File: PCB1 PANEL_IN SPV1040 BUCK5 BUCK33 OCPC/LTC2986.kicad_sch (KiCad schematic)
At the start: 1 part, among them U15 LTC2986HLX_PBF

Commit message: s
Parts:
- removed U15: LTC2986HLX_PBF, LTC2986HLX_PBF:QFP50P900X900X160-48N, symbol LTC2986:LTC2986HLX_PBF
- added C1, C4, C5, C6: 10uF, symbol Device:C
- added C2: 47uF, symbol Device:C
- added C3: 0.1uF, symbol Device:C
- added C7, C8: 1uF, symbol Device:C
- added U1: LTC2986HLX-PBF, LX_48_ADI, symbol 2025-01-09_17-24-37:LTC2986HLX-PBF
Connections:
- net GND: now also C1.2, C2.2, C3.2, C4.2, C5.2, C6.2, C7.2, C8.2, U1.1 (GND), U1.12 (GND), U1.15 (GND), U1.26 (GND), U1.27 (GND), U1.28 (GND), U1.29 (GND), U1.3 (GND), U1.30 (GND), U1.31 (GND), U1.32 (GND), U1.33 (GND), U1.34 (GND), U1.35 (GND), U1.36 (COM), U1.44 (GND), U1.5 (GND), U1.7 (GND), U1.9 (GND)
- new net: C8.1, U1.11 (VREFBYP)
- new net: C7.1, U1.13 (VREFOUT), U1.14 (VREFP)
- new net: C4.1, U1.43 (LDO)
- new net: C6.1, U1.46 (Q3)
- new net: C5.1, U1.47 (Q2), U1.48 (Q1)
- new net CS: U1.41 (*CS)
- new net INTERRUPT: U1.37 (INTERRUPT)
- new net MISO: U1.40 (SDI)
- new net MOSI: U1.39 (SDO)
- new net RST: U1.42 (*RESET)
- new net SCK: U1.38 (SCK)
- new net VDD: C1.1, C2.1, C3.1, U1.2 (VDD), U1.4 (VDD), U1.45 (VDD), U1.6 (VDD), U1.8 (VDD)
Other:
- note added: "1. RESET PIN and CS PIN are ACTIVE LOW 2. INTERRUPT pin here is an outpin which gives LOW when the conversion cycle in the process and HIGH on the conclusion"

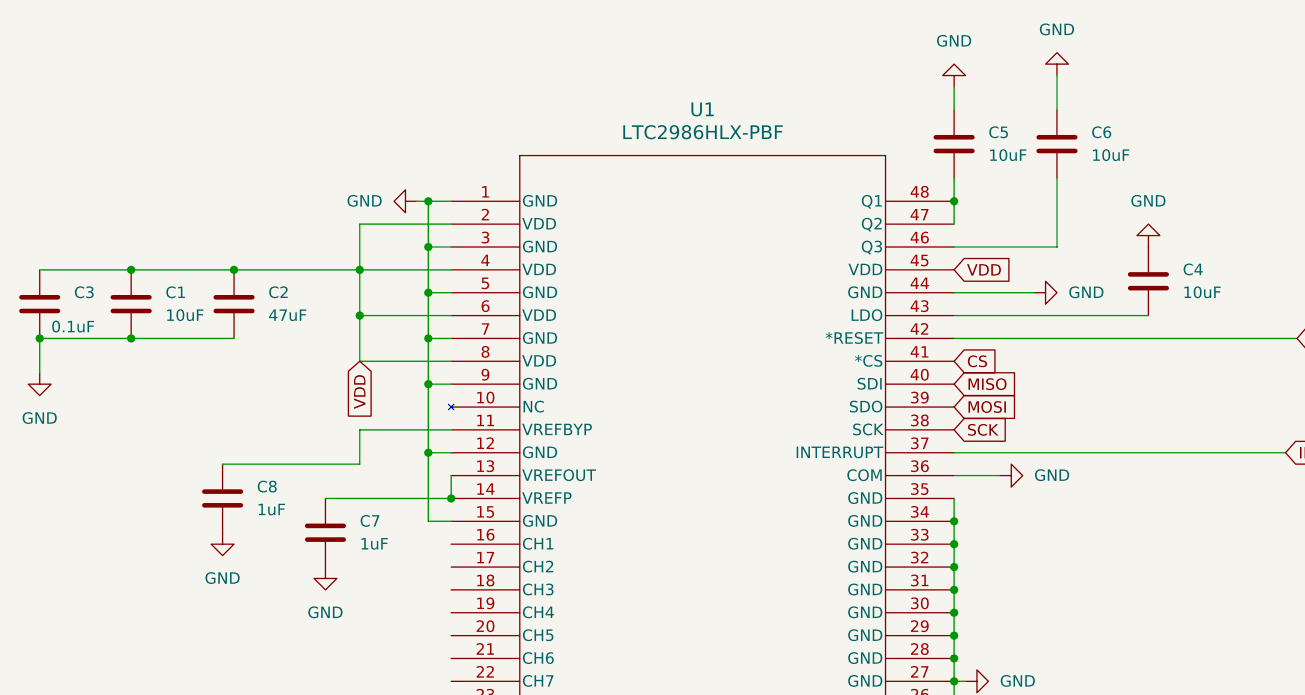
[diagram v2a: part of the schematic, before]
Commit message: Relabeling according to standards
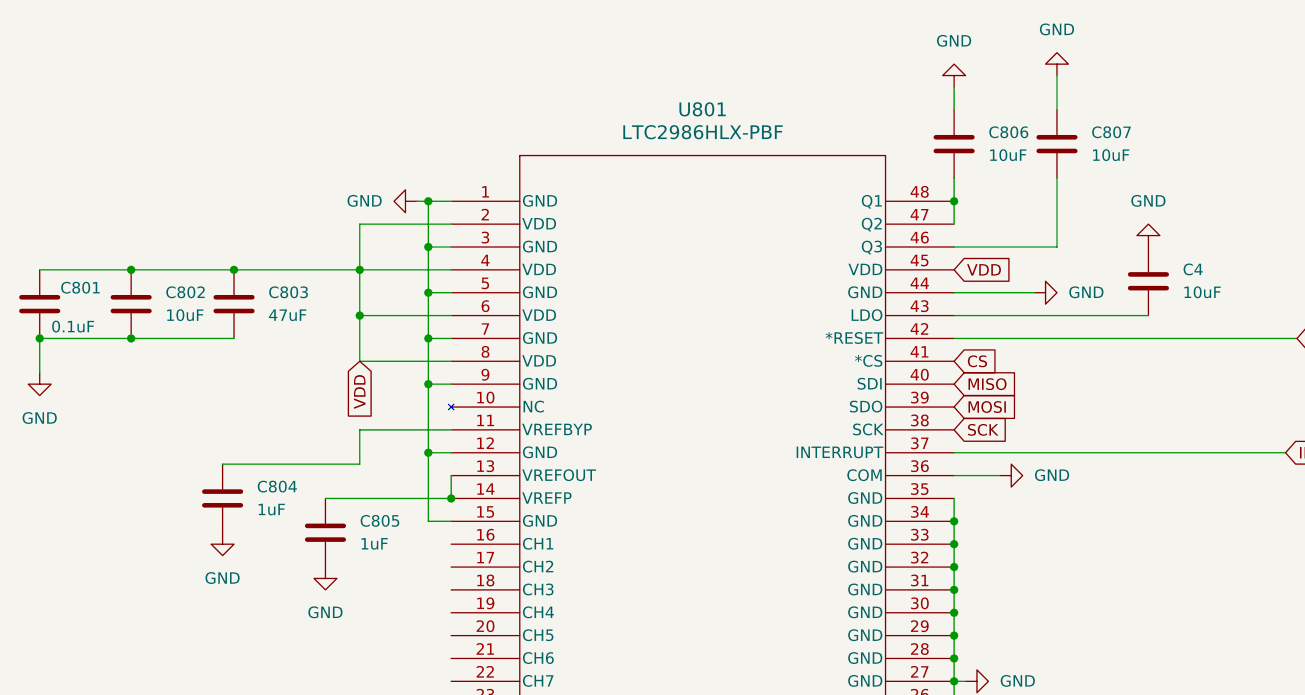
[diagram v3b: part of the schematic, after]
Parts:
- U801: renamed from U1; footprint LX_48_ADI -> (none)
- renumbered C3 to C801, C1 to C802, C2 to C803, C8 to C804, C7 to C805, C5 to C806, C6 to C807
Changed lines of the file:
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@@
 		(dnp no)
 		(fields_autoplaced yes)
-		(property "Reference" "#PWR01"
+		(property "Reference" "#PWR0111"
 			(at 97.79 38.1 0)
 			(effects
@@
 		(instances
 			(project ""
+				(path "/494c9d9f-6b33-4248-a813-27ffaaa929bd/81ba6a5a-e21d-4cec-83f0-5d840c1285ed"
+					(reference "#PWR0111")
+					(unit 1)
+				)
+			)
+			(project ""
 				(path "/e5df9c19-46f5-47d3-b6f4-a0778a1551ae"
 					(reference "#PWR01")
@@
 		(dnp no)
 		(fields_autoplaced yes)
-		(property "Reference" "U1"
+		(property "Reference" "U801"
 			(at 135.89 27.94 0)
 			(effects
@@
 			)
 		)
-		(property "Footprint" "LX_48_ADI"
+		(property "Footprint" ""
 			(at 107.95 38.1 0)
 			(effects
@@
 		(instances
 			(project ""
+				(path "/494c9d9f-6b33-4248-a813-27ffaaa929bd/81ba6a5a-e21d-4cec-83f0-5d840c1285ed"
+					(reference "U801")
+					(unit 1)
+				)
+			)
+			(project ""
 				(path "/e5df9c19-46f5-47d3-b6f4-a0778a1551ae"
 					(reference "U1")
@@
 		(dnp no)
 		(fields_autoplaced yes)
-		(property "Reference" "#PWR05"
+		(property "Reference" "#PWR0155"
 			(at 185.42 36.83 0)
 			(effects
@@
 		)
 		(instances
+			(project ""
+				(path "/494c9d9f-6b33-4248-a813-27ffaaa929bd/81ba6a5a-e21d-4cec-83f0-5d840c1285ed"
+					(reference "#PWR0155")
+					(unit 1)
+				)
+			)
 			(project "LTC2986"
 				(path "/e5df9c19-46f5-47d3-b6f4-a0778a1551ae"
@@
 		(dnp no)
 		(fields_autoplaced yes)
-		(property "Reference" "C6"
+		(property "Reference" "C807"
 			(at 179.07 30.4799 0)
 			(effects
@@
 		)
 		(instances
+			(project ""
+				(path "/494c9d9f-6b33-4248-a813-27ffaaa929bd/81ba6a5a-e21d-4cec-83f0-5d840c1285ed"
+					(reference "C807")
+					(unit 1)
+				)
+			)
 			(project "LTC2986"
 				(path "/e5df9c19-46f5-47d3-b6f4-a0778a1551ae"
@@
 		(dnp no)
 		(fields_autoplaced yes)
-		(property "Reference" "#PWR04"
+		(property "Reference" "#PWR0150"
 			(at 62.23 63.5 0)
 			(effects
@@
 		)
 		(instances
+			(project ""
+				(path "/494c9d9f-6b33-4248-a813-27ffaaa929bd/81ba6a5a-e21d-4cec-83f0-5d840c1285ed"
+					(reference "#PWR0150")
+					(unit 1)
+				)
+			)
 			(project "LTC2986"
 				(path "/e5df9c19-46f5-47d3-b6f4-a0778a1551ae"
@@
 		(dnp no)
 		(fields_autoplaced yes)
-		(property "Reference" "C5"
+		(property "Reference" "C806"
 			(at 167.64 30.4799 0)
 			(effects
@@
 		)
 		(instances
+			(project ""
+				(path "/494c9d9f-6b33-4248-a813-27ffaaa929bd/81ba6a5a-e21d-4cec-83f0-5d840c1285ed"
+					(reference "C806")
+					(unit 1)
+				)
+			)
 			(project "LTC2986"
 				(path "/e5df9c19-46f5-47d3-b6f4-a0778a1551ae"
@@
 		(dnp no)
 		(fields_autoplaced yes)
-		(property "Reference" "C2"
+		(property "Reference" "C803"
 			(at 87.63 48.2599 0)
 			(effects
@@
 		)
 		(instances
+			(project ""
+				(path "/494c9d9f-6b33-4248-a813-27ffaaa929bd/81ba6a5a-e21d-4cec-83f0-5d840c1285ed"
+					(reference "C803")
+					(unit 1)
+				)
+			)
 			(project "LTC2986"
 				(path "/e5df9c19-46f5-47d3-b6f4-a0778a1551ae"
@@
 		(dnp no)
 		(fields_autoplaced yes)
-		(property "Reference" "C8"
+		(property "Reference" "C804"
 			(at 86.36 69.8499 0)
 			(effects
@@
 		)
 		(instances
+			(project ""
+				(path "/494c9d9f-6b33-4248-a813-27ffaaa929bd/81ba6a5a-e21d-4cec-83f0-5d840c1285ed"
+					(reference "C804")
+					(unit 1)
+				)
+			)
 			(project "LTC2986"
 				(path "/e5df9c19-46f5-47d3-b6f4-a0778a1551ae"
@@
 		(dnp no)
 		(fields_autoplaced yes)
-		(property "Reference" "#PWR02"
+		(property "Reference" "#PWR0151"
 			(at 171.45 91.44 0)
 			(effects
@@
 		)
 		(instances
+			(project ""
+				(path "/494c9d9f-6b33-4248-a813-27ffaaa929bd/81ba6a5a-e21d-4cec-83f0-5d840c1285ed"
+					(reference "#PWR0151")
+					(unit 1)
+				)
+			)
 			(project "LTC2986"
 				(path "/e5df9c19-46f5-47d3-b6f4-a0778a1551ae"
@@
 		(dnp no)
 		(fields_autoplaced yes)
-		(property "Reference" "C1"
+		(property "Reference" "C802"
 			(at 76.2 48.2599 0)
 			(effects
@@
 		(instances
 			(project ""
+				(path "/494c9d9f-6b33-4248-a813-27ffaaa929bd/81ba6a5a-e21d-4cec-83f0-5d840c1285ed"
+					(reference "C802")
+					(unit 1)
+				)
+			)
+			(project ""
 				(path "/e5df9c19-46f5-47d3-b6f4-a0778a1551ae"
 					(reference "C1")
@@
 		(dnp no)
 		(fields_autoplaced yes)
-		(property "Reference" "#PWR03"
+		(property "Reference" "#PWR0156"
 			(at 179.07 48.26 0)
 			(effects
@@
 		)
 		(instances
+			(project ""
+				(path "/494c9d9f-6b33-4248-a813-27ffaaa929bd/81ba6a5a-e21d-4cec-83f0-5d840c1285ed"
+					(reference "#PWR0156")
+					(unit 1)
+				)
+			)
 			(project "LTC2986"
 				(path "/e5df9c19-46f5-47d3-b6f4-a0778a1551ae"
@@
 		(dnp no)
 		(fields_autoplaced yes)
-		(property "Reference" "C7"
+		(property "Reference" "C805"
 			(at 97.79 73.6599 0)
 			(effects
@@
 		)
 		(instances
+			(project ""
+				(path "/494c9d9f-6b33-4248-a813-27ffaaa929bd/81ba6a5a-e21d-4cec-83f0-5d840c1285ed"
+					(reference "C805")
+					(unit 1)
+				)
+			)
 			(project "LTC2986"
 				(path "/e5df9c19-46f5-47d3-b6f4-a0778a1551ae"
@@
 		(dnp no)
 		(fields_autoplaced yes)
-		(property "Reference" "#PWR09"
+		(property "Reference" "#PWR0158"
 			(at 93.98 85.09 0)
 			(effects
@@
 		)
 		(instances
+			(project ""
+				(path "/494c9d9f-6b33-4248-a813-27ffaaa929bd/81ba6a5a-e21d-4cec-83f0-5d840c1285ed"
+					(reference "#PWR0158")
+					(unit 1)
+				)
+			)
 			(project "LTC2986"
 				(path "/e5df9c19-46f5-47d3-b6f4-a0778a1551ae"
@@
 		(dnp no)
 		(fields_autoplaced yes)
-		(property "Reference" "#PWR010"
+		(property "Reference" "#PWR0157"
 			(at 82.55 81.28 0)
 			(effects
@@
 		)
 		(instances
+			(project ""
+				(path "/494c9d9f-6b33-4248-a813-27ffaaa929bd/81ba6a5a-e21d-4cec-83f0-5d840c1285ed"
+					(reference "#PWR0157")
+					(unit 1)
+				)
+			)
 			(project "LTC2986"
 				(path "/e5df9c19-46f5-47d3-b6f4-a0778a1551ae"
@@
 		(on_board yes)
 		(dnp no)
-		(property "Reference" "C3"
-			(at 66.04 48.2599 0)
+		(property "Reference" "C801"
+			(at 64.516 47.752 0)
 			(effects
 				(font
@@
 		)
 		(instances
+			(project ""
+				(path "/494c9d9f-6b33-4248-a813-27ffaaa929bd/81ba6a5a-e21d-4cec-83f0-5d840c1285ed"
+					(reference "C801")
+					(unit 1)
+				)
+			)
 			(project "LTC2986"
 				(path "/e5df9c19-46f5-47d3-b6f4-a0778a1551ae"
@@
 		(dnp no)
 		(fields_autoplaced yes)
-		(property "Reference" "#PWR06"
+		(property "Reference" "#PWR0153"
 			(at 163.83 19.05 0)
 			(effects
@@
 		)
 		(instances
+			(project ""
+				(path "/494c9d9f-6b33-4248-a813-27ffaaa929bd/81ba6a5a-e21d-4cec-83f0-5d840c1285ed"
+					(reference "#PWR0153")
+					(unit 1)
+				)
+			)
 			(project "LTC2986"
 				(path "/e5df9c19-46f5-47d3-b6f4-a0778a1551ae"
@@
 		(dnp no)
 		(fields_autoplaced yes)
-		(property "Reference" "#PWR07"
+		(property "Reference" "#PWR0154"
 			(at 175.26 17.78 0)
 			(effects
@@
 		)
 		(instances
+			(project ""
+				(path "/494c9d9f-6b33-4248-a813-27ffaaa929bd/81ba6a5a-e21d-4cec-83f0-5d840c1285ed"
+					(reference "#PWR0154")
+					(unit 1)
+				)
+			)
 			(project "LTC2986"
 				(path "/e5df9c19-46f5-47d3-b6f4-a0778a1551ae"
@@
 		(dnp no)
 		(fields_autoplaced yes)
-		(property "Reference" "#PWR08"
+		(property "Reference" "#PWR0152"
 			(at 175.26 68.58 0)
 			(effects
@@
 		)
 		(instances
-			(project "LTC2986"
-				(path "/e5df9c19-46f5-47d3-b6f4-a0778a1551ae"
+			(project ""
+				(path "/494c9d9f-6b33-4248-a813-27ffaaa929bd/81ba6a5a-e21d-4cec-83f0-5d840c1285ed"
+					(reference "#PWR0152")
+					(unit 1)
+				)
+			)
+			(project "LTC2986"
+				(path "/e5df9c19-46f5-47d3-b6f4-a0778a1551ae"
